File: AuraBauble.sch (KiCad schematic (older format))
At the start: 37 parts, among them J1 Bauble-Expando!, J2 USB_A, J3 SWD, SW1 KXT 321 LHS, U1 ATSAMD11D14A-M, U2 LP5912-3.3DRV, U3 74LVC1G02SE-7, U4 NXB0104GU12X, Y1 FC-135R

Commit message: Update some annotations.
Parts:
- renumbered D6 to D2
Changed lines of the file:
@@
 Programmer may\nhave pullup.
 $Comp
-L dk_TVS-Diodes:PRTR5V0U2X_215 D6
+L dk_TVS-Diodes:PRTR5V0U2X_215 D2
 U 1 1 5F64F554
 P 10550 1450
-F 0 "D6" V 10750 1050 60  0000 L CNN
+F 0 "D2" V 10750 1050 60  0000 L CNN
 F 1 "PRTR5V0U2X_215" H 10200 1800 60  0000 L CNN
 F 2 "digikey-footprints:TO-253-4" H 10750 1650 60  0001 L CNN

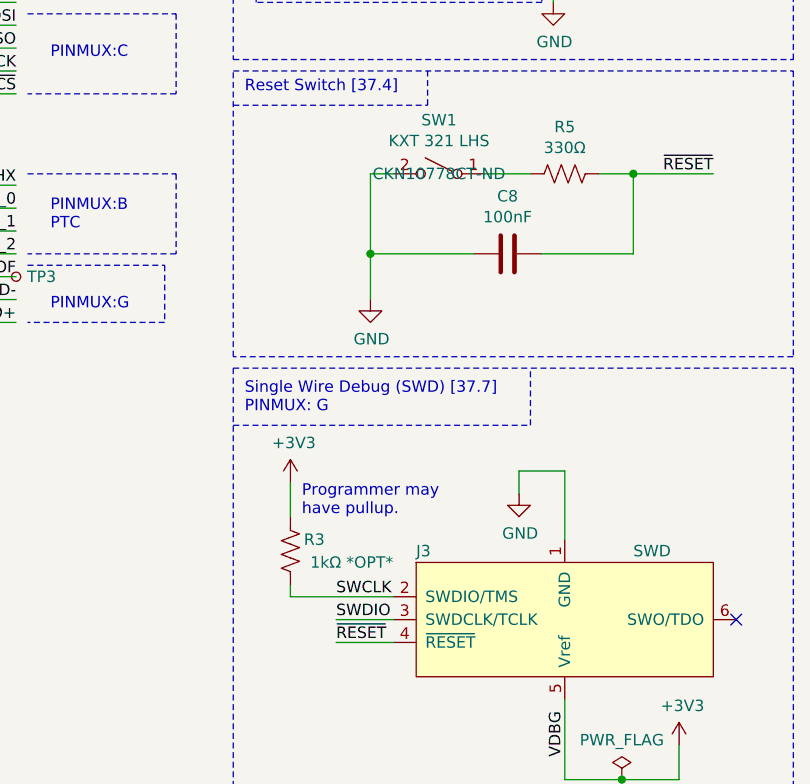
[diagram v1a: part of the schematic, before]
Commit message: Somebody had SWDIO/SWCLK swapped.
It's me. I'm somebody.
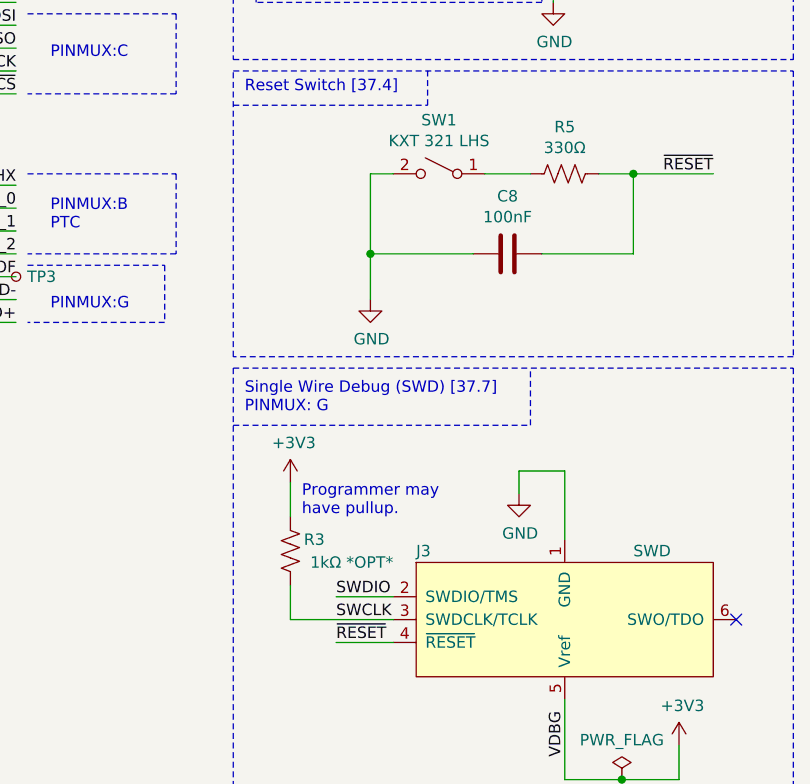
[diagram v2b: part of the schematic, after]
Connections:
- net SWCLK: now also J3.3 (SWDCLK/TCLK); no longer J3.2 (SWDIO/TMS)
- net SWDIO: now also J3.2 (SWDIO/TMS); no longer J3.3 (SWDCLK/TCLK)
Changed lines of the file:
@@
 F 2 "Button_Switch_SMD:SW_SPST_CK_KXT3" H 9600 2950 50  0001 C CNN
 F 3 "~" H 9600 2950 50  0001 C CNN
-F 4 "CKN10778CT-ND" H 9600 2950 50  0000 C CNN "Digi-Key"
+F 4 "CKN10778CT-ND" H 9600 2950 50  0001 C CNN "Digi-Key"
 	1    9600 2950
 	-1   0    0    -1
@@
 	10650 5600 10650 5450
 Wire Wire Line
-	9400 4800 8950 4800
-Wire Wire Line
-	9400 4900 9150 4900
+	9400 4900 8950 4900
+Wire Wire Line
+	9400 4800 9150 4800
 Wire Wire Line
 	9400 5000 9150 5000
@@
 Text Label 5850 2600 0    50   ~ 0
 SWDIO
+Text Label 9150 4900 0    50   ~ 0
+SWCLK
 Text Label 9150 4800 0    50   ~ 0
-SWCLK
-Text Label 9150 4900 0    50   ~ 0
 SWDIO
 NoConn ~ 10900 4900
 Wire Wire Line
-	8950 4800 8950 4750
+	8950 4900 8950 4750
 $Comp
 L Device:R_US R3

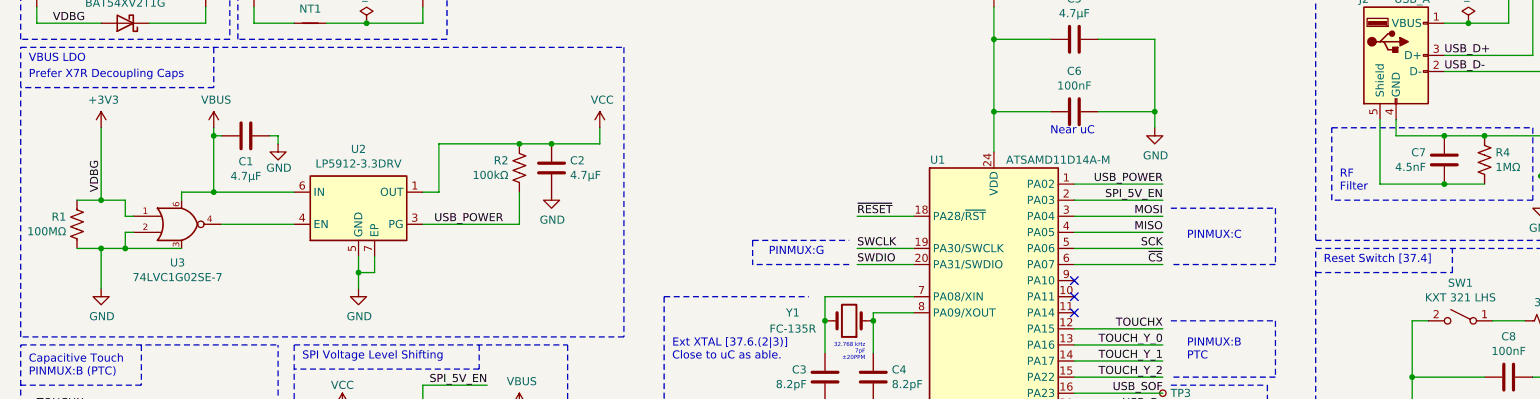
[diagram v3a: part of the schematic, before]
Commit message: Cleanup some C & R values.
Adjusted C7 up slightly based on parts available. R1 moved from 100 MOhms to 1 MOhm to line up part with R4.
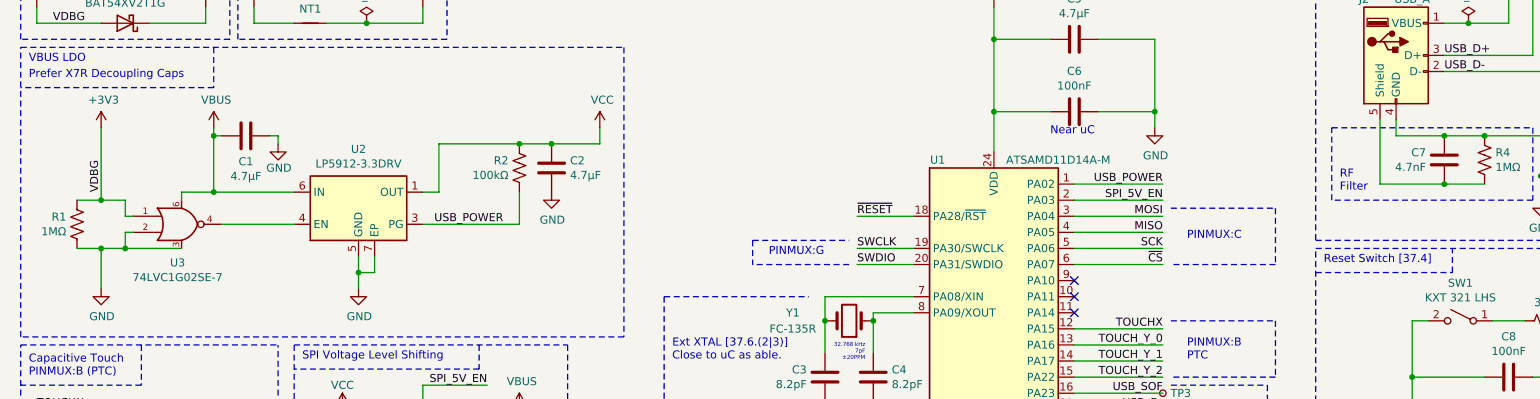
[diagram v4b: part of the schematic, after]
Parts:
- C7: value 4.5nF -> 4.7nF
- R1: value 100MΩ -> 1MΩ
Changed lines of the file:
@@
 Sheet 1 1
 Title "Aura Bauble"
-Date "2020-09-14"
+Date "2020-09-15"
 Rev "0"
 Comp "cmd.wtf"
@@
 P 9500 1950
 F 0 "C7" H 9386 1996 50  0000 R CNN
-F 1 "4.5nF" H 9386 1905 50  0000 R CNN
+F 1 "4.7nF" H 9386 1905 50  0000 R CNN
 F 2 "Capacitor_SMD:C_0402_1005Metric" H 9538 1800 50  0001 C CNN
 F 3 "~" H 9500 1950 50  0001 C CNN
@@
 P 1000 2350
 F 0 "R1" H 1067 2304 50  0000 L CNN
-F 1 "100MΩ" H 1067 2395 50  0000 L CNN
+F 1 "1MΩ" H 1067 2395 50  0000 L CNN
 F 2 "Resistor_SMD:R_0402_1005Metric" V 1040 2340 50  0001 C CNN
 F 3 "~" H 1000 2350 50  0001 C CNN
